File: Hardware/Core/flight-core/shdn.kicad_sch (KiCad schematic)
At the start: 19 parts, among them J101 Conn_01x02, J21 Conn_01x02, J22 Conn_01x02, J23 Conn_01x02, J24 Conn_01x02, J25 Conn_01x02, J26 Conn_01x02, J27 Conn_01x02, J28 Conn_01x02, J29 Conn_01x02, J3 Conn_01x02, J4 Conn_01x02, J6 Conn_01x02, J7 Conn_01x02, U10 LTV-356T, U65 LTV-356T

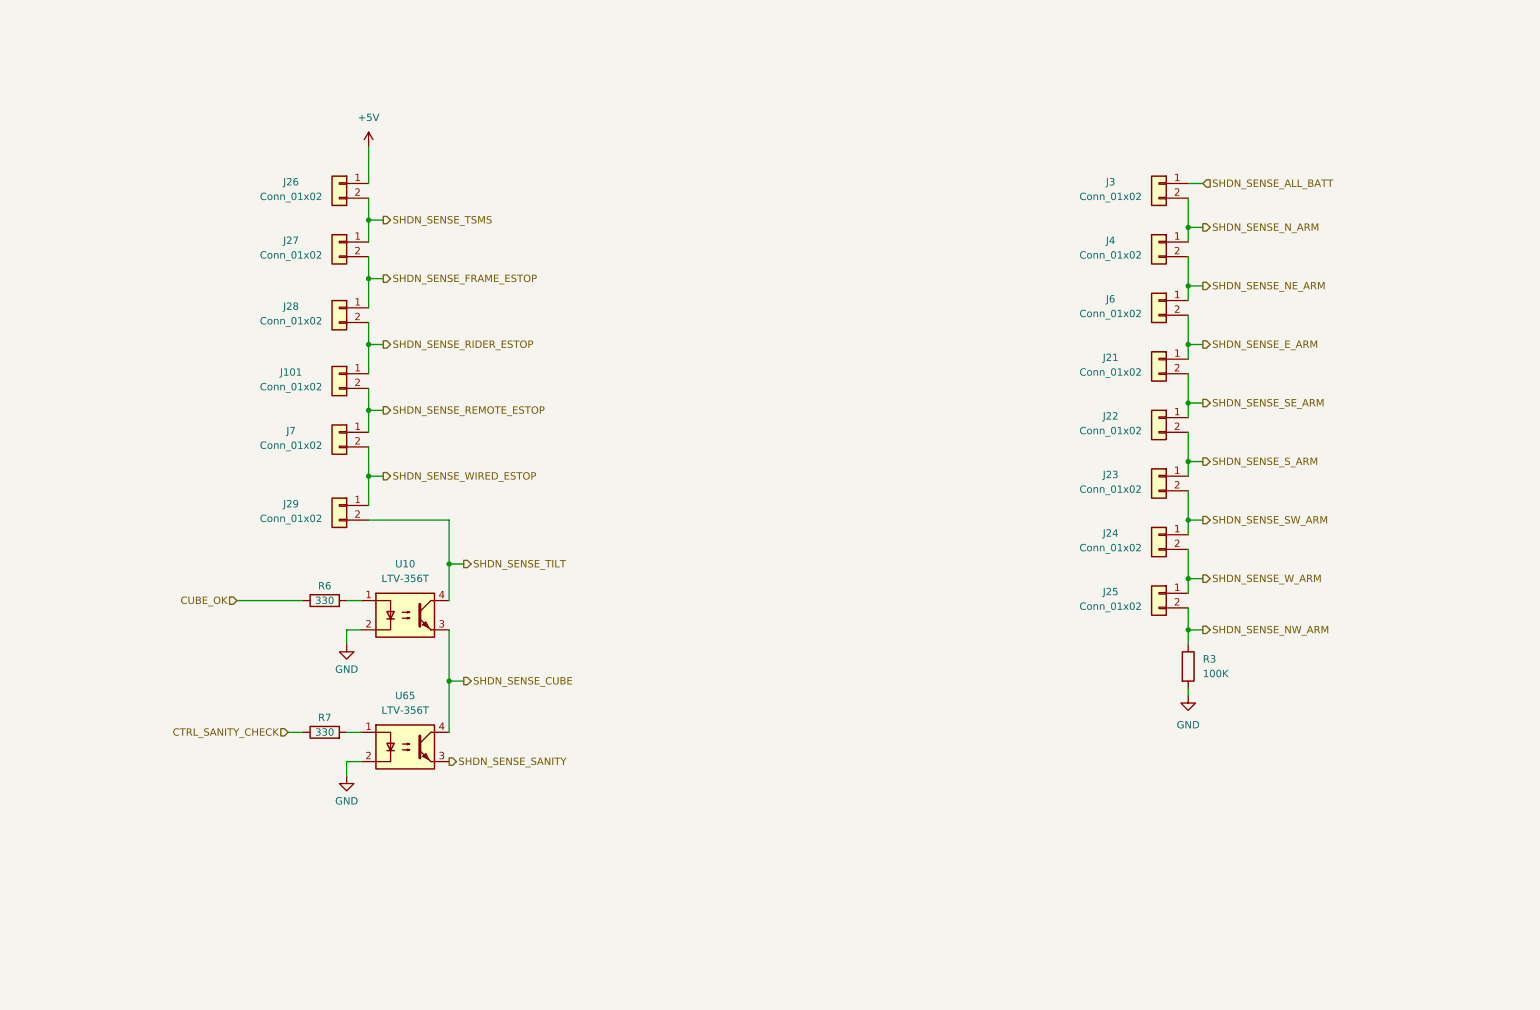
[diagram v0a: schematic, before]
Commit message: added all cube pins and corrected cube shdn node
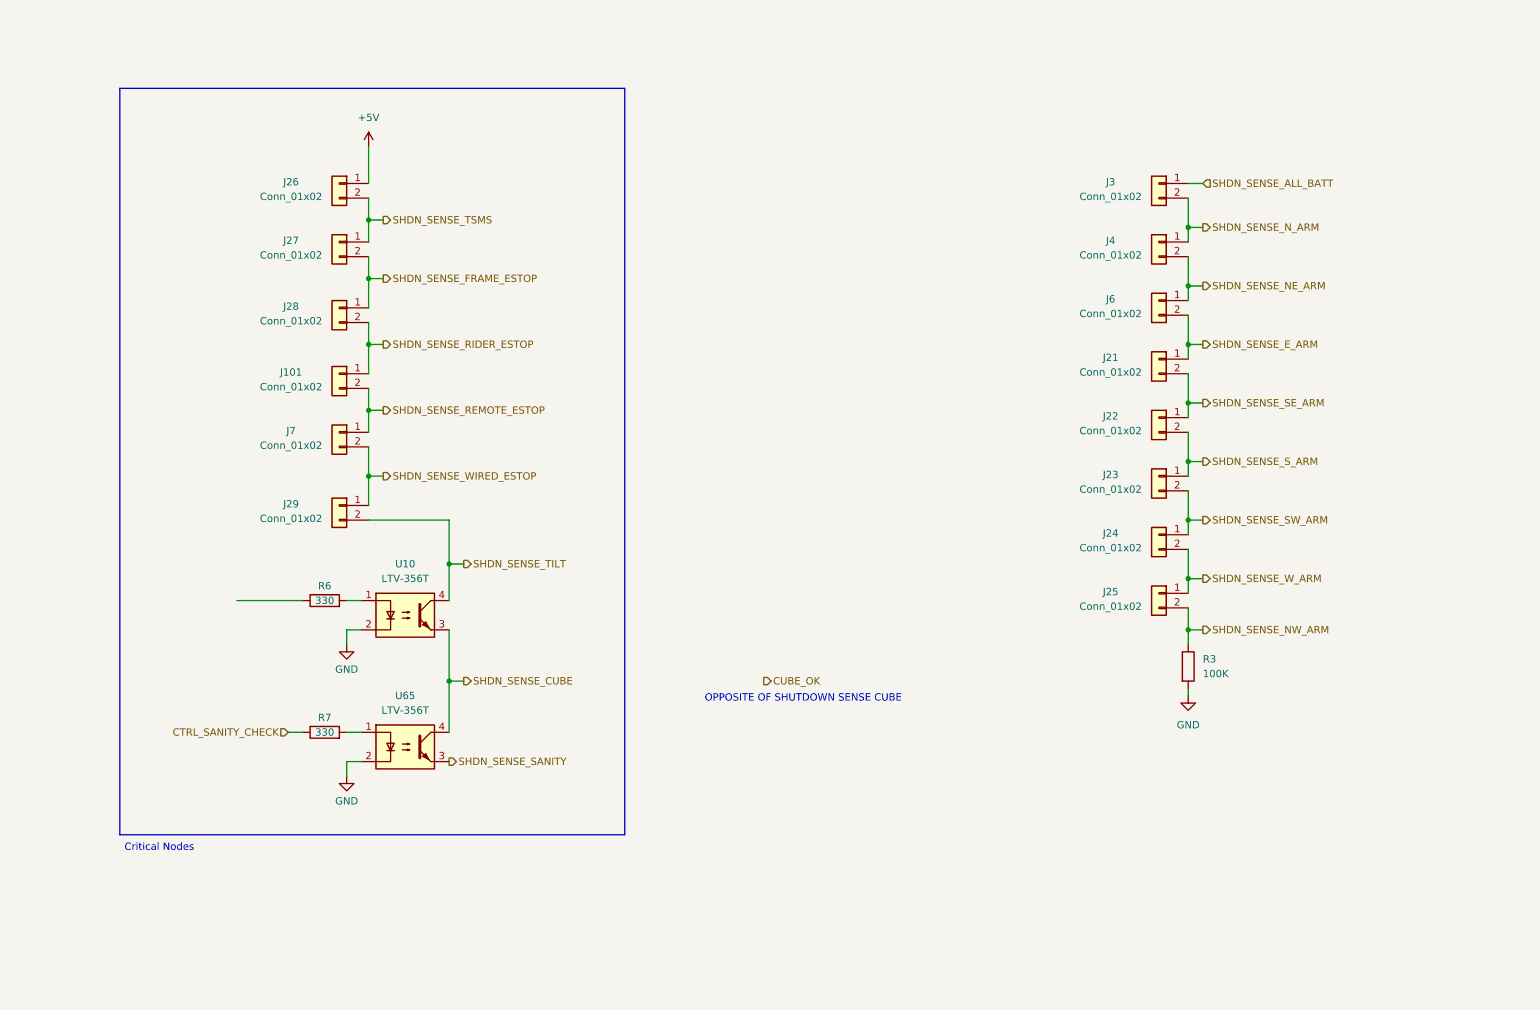
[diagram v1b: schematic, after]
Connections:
- net CUBE_OK: no longer R6.1
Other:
- note added: "Critical Nodes"
- note added: "OPPOSITE OF SHUTDOWN SENSE CUBE"
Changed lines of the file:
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@@
 	(generator_version "9.0")
 	(paper "A4")
+	(rectangle
+		(start 34.29 27.94)
+		(end 121.92 157.48)
+		(stroke
+			(width 0)
+			(type default)
+		)
+		(fill
+			(type none)
+		)
+	)
+	(text "OPPOSITE OF SHUTDOWN SENSE CUBE"
+		(exclude_from_sim no)
+		(at 152.908 133.858 0)
+		(effects
+			(font
+				(size 1.27 1.27)
+			)
+		)
+	)
+	(text "Critical Nodes"
+		(exclude_from_sim no)
+		(at 41.148 159.766 0)
+		(effects
+			(font
+				(size 1.27 1.27)
+			)
+		)
+	)
 	(junction
 		(at 219.71 72.39)
@@
 	)
 	(hierarchical_label "CUBE_OK"
-		(shape input)
-		(at 54.61 116.84 180)
+		(shape output)
+		(at 146.05 130.81 0)
 		(effects
 			(font
 				(size 1.27 1.27)
 			)
-			(justify right)
-		)
-	)
+			(justify left)
+		)
+	)

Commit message: reordered shutdown nodes
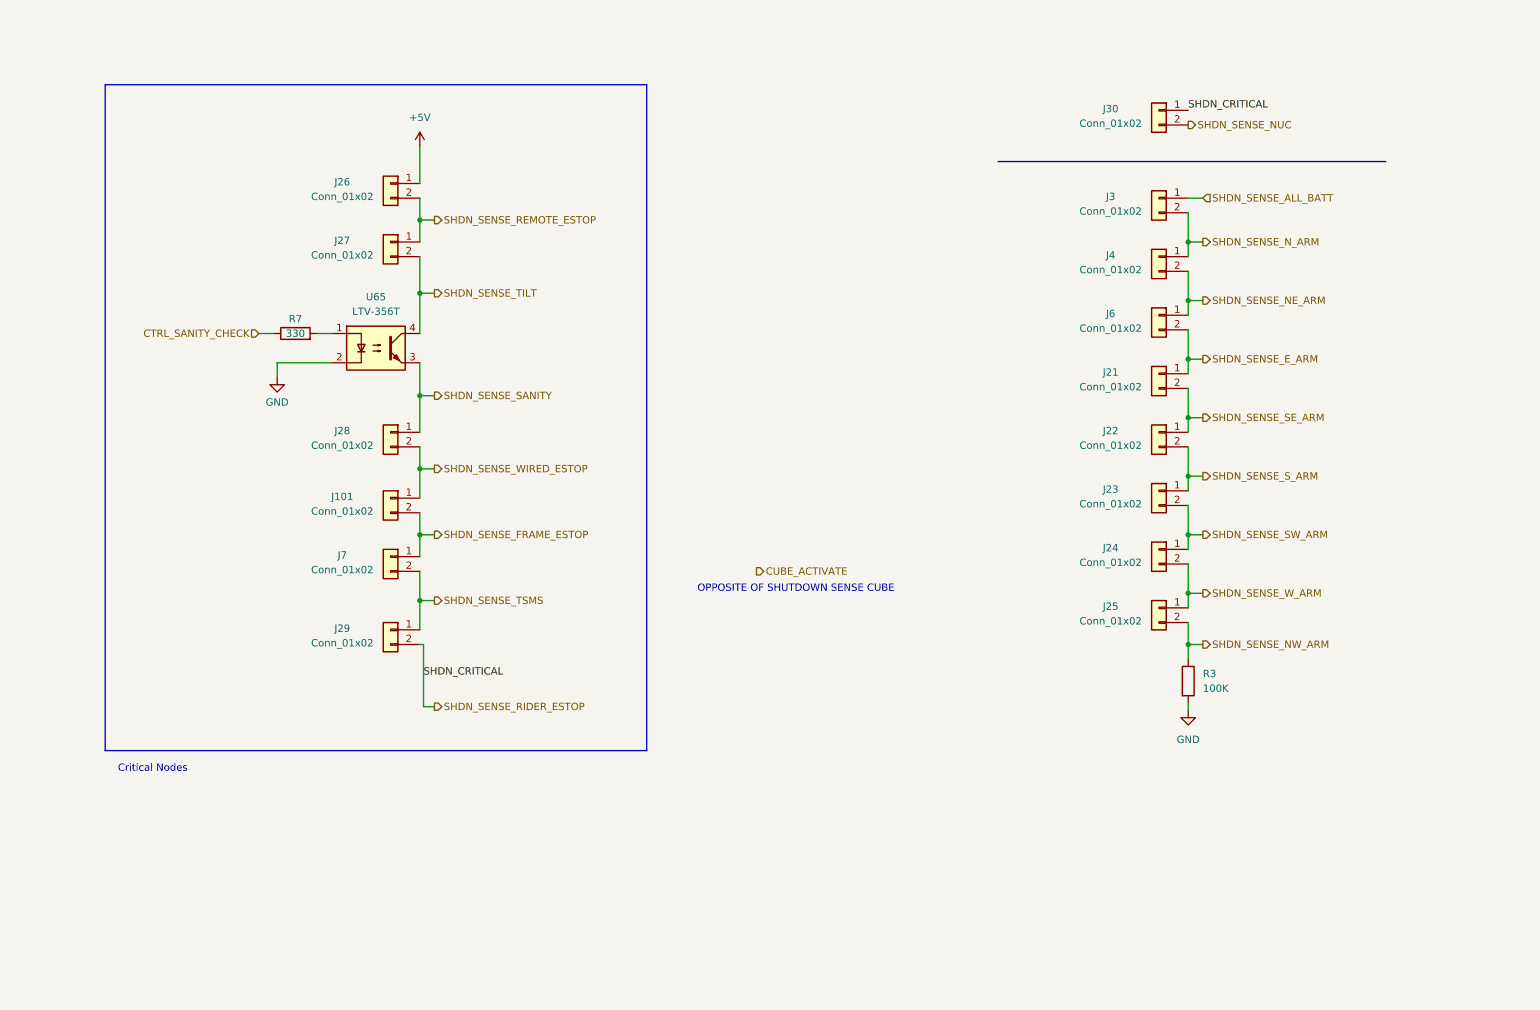
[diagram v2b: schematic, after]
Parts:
- removed R6: 330, OEM:R_0603_1608Metric, symbol OEM:1KR
- removed U10: LTV-356T, Package_SO:SO-4_4.4x3.6mm_P2.54mm, symbol Isolator:LTV-356T
- added J30: Conn_01x02, symbol Connector_Generic:Conn_01x02
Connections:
- net SHDN_SENSE_CUBE is gone; now on net SHDN_SENSE_TILT: U65.4
- net SHDN_SENSE_FRAME_ESTOP: now also J101.2 (Pin_2), J7.1 (Pin_1); no longer J27.2 (Pin_2), J28.1 (Pin_1)
- net SHDN_SENSE_REMOTE_ESTOP: now also J26.2 (Pin_2), J27.1 (Pin_1); no longer J101.2 (Pin_2), J7.1 (Pin_1)
- net SHDN_SENSE_RIDER_ESTOP: now also J29.2 (Pin_2), J30.1 (Pin_1); no longer J101.1 (Pin_1), J28.2 (Pin_2)
- net SHDN_SENSE_SANITY: now also J28.1 (Pin_1)
- net SHDN_SENSE_TILT: now also J27.2 (Pin_2); no longer J29.2 (Pin_2)
- net SHDN_SENSE_TSMS: now also J29.1 (Pin_1), J7.2 (Pin_2); no longer J26.2 (Pin_2), J27.1 (Pin_1)
- net SHDN_SENSE_WIRED_ESTOP: now also J101.1 (Pin_1), J28.2 (Pin_2); no longer J29.1 (Pin_1), J7.2 (Pin_2)
- new net SHDN_SENSE_NUC: J30.2 (Pin_2)
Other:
- moved on the sheet: J101, J21, J22, J23, J24, J25, J26, J27, J28, J29, J3, J4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

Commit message: top sheet reorg
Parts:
- added Q16: MMBF170, TO_SOT_Packages_SMD:SOT-23, symbol formula:MMBF170
- added R97: 100K, footprints:R_0805_OEM, symbol formula:R_100K
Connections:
- net +5V: now also R97.1
- net CUBE_ACTIVATE: now also Q16.3 (D), R97.2
- net GND: now also Q16.2 (S)
- net SHDN_SENSE_NW_ARM: now also Q16.1 (G)
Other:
- note added: "BATTERY SHDNS (x4)"
- note added: "CRITICAL NODES"
- note removed: "Critical Nodes"
- note removed: "OPPOSITE OF SHUTDOWN SENSE CUBE"
- moved on the sheet: J21, J22, J23, J24, J25, J3, J30, J4, J6, R3

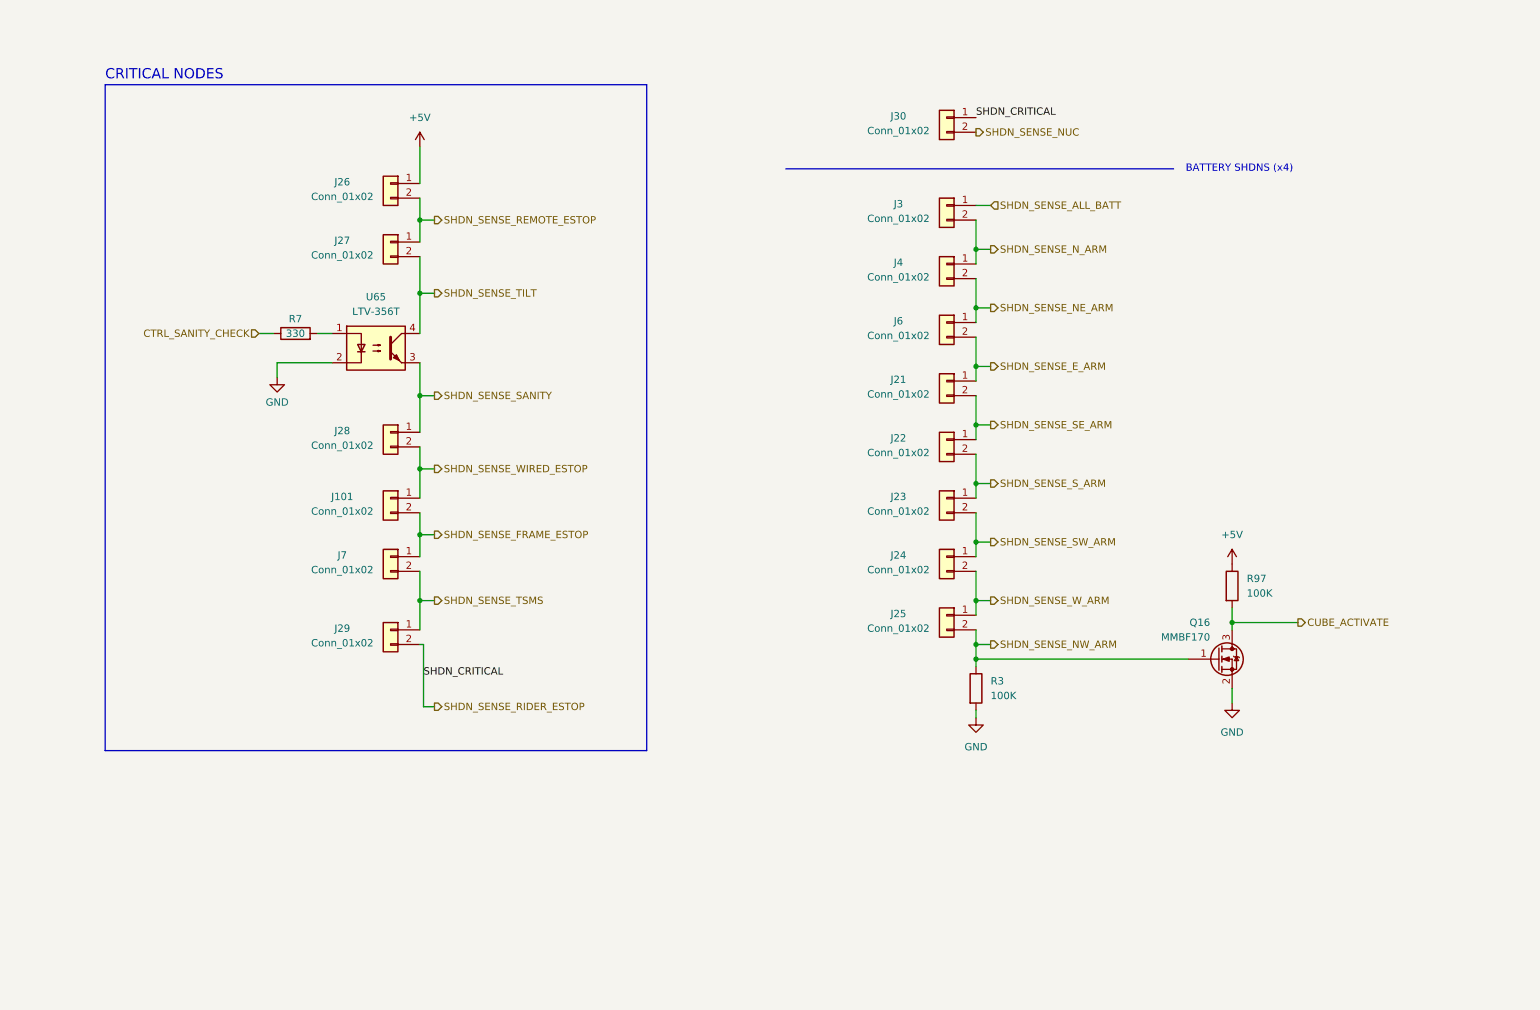
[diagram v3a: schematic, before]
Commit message: updated shutdown and some aux circuits
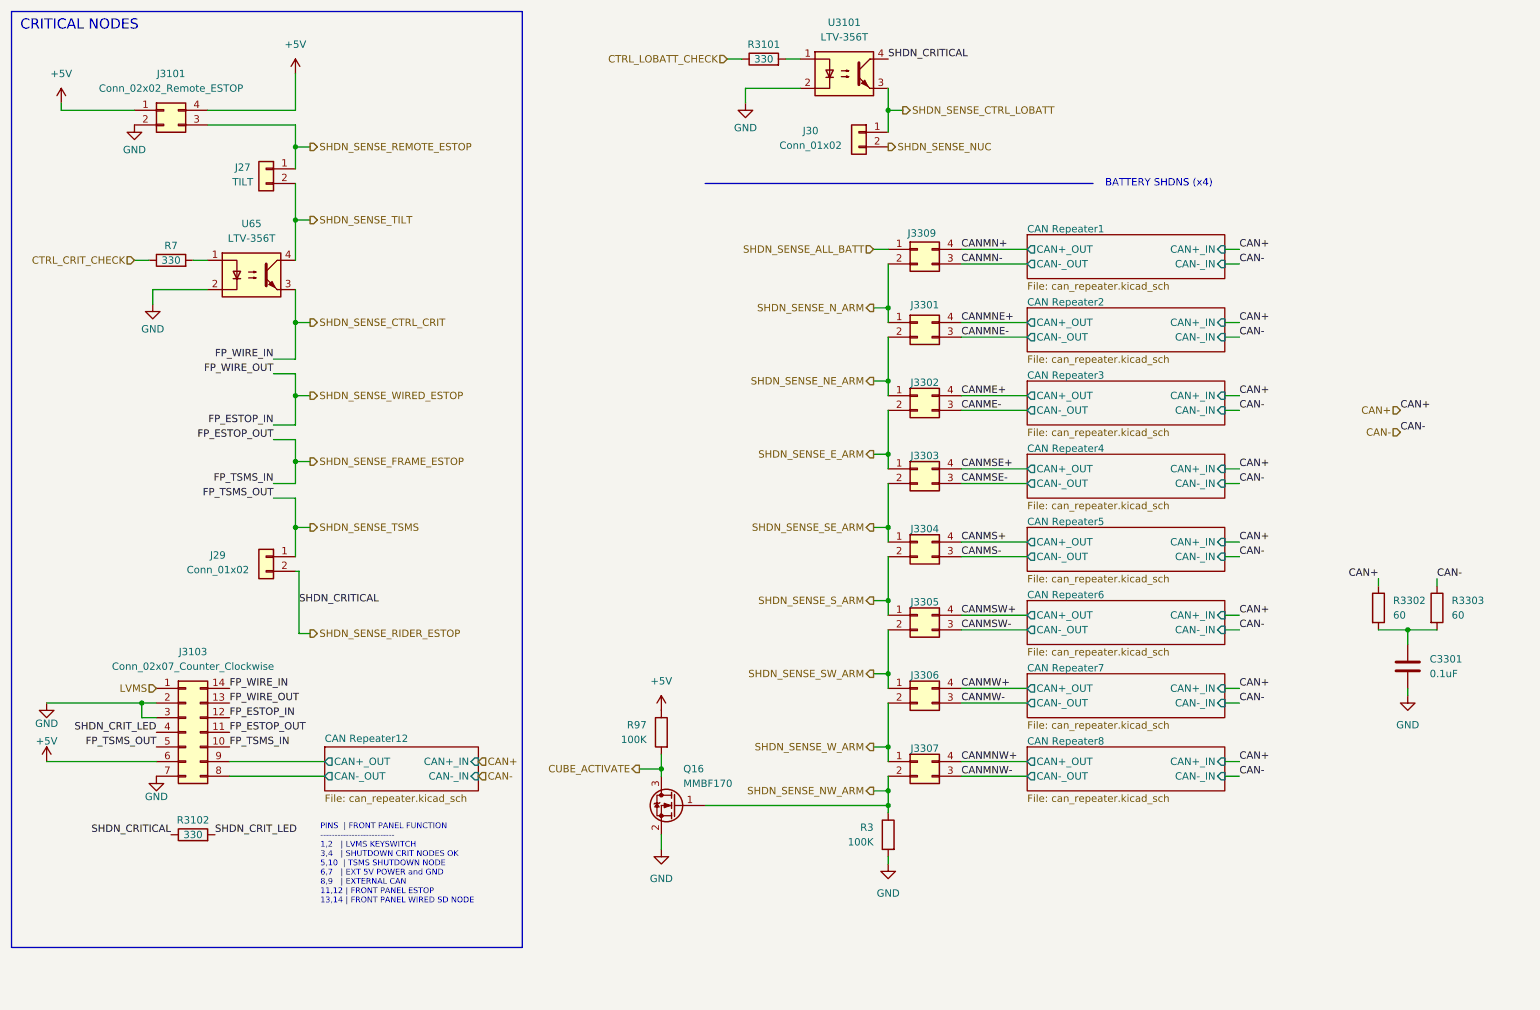
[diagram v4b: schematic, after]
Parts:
- removed J101, J21, J22, J23, J24, J25, J26, J28, J3, J4, J6, J7: Conn_01x02, symbol Connector_Generic:Conn_01x02
- added C3301: 0.1uF, footprints:C_0603_1608Metric, symbol OlinBAD:C_0.1uF_0603
- added J3101, J3301, J3302, J3303, J3304, J3305, J3306, J3307, J3309: Conn_02x02_Remote_ESTOP, Connector_Molex:Molex_Micro-Fit_3.0_43045-0400_2x02_P3.00mm_Horizontal, symbol Connector_Generic:Conn_02x02_Counter_Clockwise
- added J3103: Conn_02x07_Counter_Clockwise, symbol Connector_Generic:Conn_02x07_Counter_Clockwise
- added R3101, R3102: 330, OEM:R_0603_1608Metric, symbol OEM:1KR
- added R3302, R3303: 60, footprints:C_0603_1608Metric, symbol Device:R
- added U3101: LTV-356T, Package_SO:SO-4_4.4x3.6mm_P2.54mm, symbol Isolator:LTV-356T
- J27: value Conn_01x02 -> TILT
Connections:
- net +5V: now also J3101.1 (Pin_1), J3101.4 (Pin_4), J3103.6 (Pin_6)
- net GND: now also C3301.2, J3101.2 (Pin_2), J3103.2 (Pin_2), J3103.3 (Pin_3), J3103.7 (Pin_7), U3101.2
- net SHDN_SENSE_ALL_BATT: now also J3309.1 (Pin_1)
- net SHDN_SENSE_E_ARM: now also J3302.2 (Pin_2), J3303.1 (Pin_1)
- net SHDN_SENSE_FRAME_ESTOP: now also J3103.10 (Pin_10), J3103.11 (Pin_11)
- net SHDN_SENSE_NE_ARM: now also J3301.2 (Pin_2), J3302.1 (Pin_1)
- net SHDN_SENSE_NW_ARM: now also J3307.2 (Pin_2)
- net SHDN_SENSE_N_ARM: now also J3301.1 (Pin_1), J3309.2 (Pin_2)
- net SHDN_SENSE_REMOTE_ESTOP: now also J3101.3 (Pin_3)
- net SHDN_SENSE_RIDER_ESTOP: now also R3102.1, U3101.4; no longer J30.1 (Pin_1)
- net SHDN_SENSE_SE_ARM: now also J3303.2 (Pin_2), J3304.1 (Pin_1)
- net SHDN_SENSE_SW_ARM: now also J3305.2 (Pin_2), J3306.1 (Pin_1)
- net SHDN_SENSE_S_ARM: now also J3304.2 (Pin_2), J3305.1 (Pin_1)
- net SHDN_SENSE_TSMS: now also J3103.5 (Pin_5)
- net SHDN_SENSE_WIRED_ESTOP: now also J3103.12 (Pin_12), J3103.13 (Pin_13)
- net SHDN_SENSE_W_ARM: now also J3306.2 (Pin_2), J3307.1 (Pin_1)
- net CTRL_SANITY_CHECK renamed CTRL_CRIT_CHECK
- net SHDN_SENSE_SANITY renamed SHDN_SENSE_CTRL_CRIT
- net SHDN_SENSE_CTRL_CRIT: now also J3103.14 (Pin_14)
- new net: C3301.1, R3302.2, R3303.2
- new net: R3101.2, U3101.1
- new net CAN Repeater12/CAN+_OUT: J3103.9 (Pin_9)
- new net CAN Repeater12/CAN-_OUT: J3103.8 (Pin_8)
- new net CAN+: R3302.1
- new net CAN-: R3303.1
- new net CANME+: J3302.4 (Pin_4)
- new net CANME-: J3302.3 (Pin_3)
- new net CANMN+: J3309.4 (Pin_4)
- new net CANMN-: J3309.3 (Pin_3)
- new net CANMNE+: J3301.4 (Pin_4)
- new net CANMNE-: J3301.3 (Pin_3)
- new net CANMNW+: J3307.4 (Pin_4)
- new net CANMNW-: J3307.3 (Pin_3)
- new net CANMS+: J3304.4 (Pin_4)
- new net CANMS-: J3304.3 (Pin_3)
- new net CANMSE+: J3303.4 (Pin_4)
- new net CANMSE-: J3303.3 (Pin_3)
- new net CANMSW+: J3305.4 (Pin_4)
- new net CANMSW-: J3305.3 (Pin_3)
- new net CANMW+: J3306.4 (Pin_4)
- new net CANMW-: J3306.3 (Pin_3)
- new net CTRL_LOBATT_CHECK: R3101.1
- new net LVMS: J3103.1 (Pin_1)
- new net SHDN_CRIT_LED: J3103.4 (Pin_4), R3102.2
- new net SHDN_SENSE_CTRL_LOBATT: J30.1 (Pin_1), U3101.3
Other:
- added sheet CAN Repeater1 (can_repeater.kicad_sch)
- added sheet CAN Repeater12 (can_repeater.kicad_sch)
- added sheet CAN Repeater2 (can_repeater.kicad_sch)
- added sheet CAN Repeater3 (can_repeater.kicad_sch)
- added sheet CAN Repeater4 (can_repeater.kicad_sch)
- added sheet CAN Repeater5 (can_repeater.kicad_sch)
- added sheet CAN Repeater6 (can_repeater.kicad_sch)
- added sheet CAN Repeater7 (can_repeater.kicad_sch)
- added sheet CAN Repeater8 (can_repeater.kicad_sch)
- note added: "PINS | FRONT PANEL FUNCTION -------------------------- 1,2 | LVMS KEYSWITCH 3,4 | SHUTDOWN CRIT NODES OK 5,10 | TSMS SHUTDOWN NODE 6,7 | EXT 5V POWER and GND 8,9 | EXTERNAL CAN 11,12 | FRONT PANEL ESTOP 13,14 | FRONT PANEL WIRED SD NODE"
- moved on the sheet: J27, J29, J30, Q16, R3, R7, R97, U65

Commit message: updated all top sheets
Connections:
- net CTRL_LOBATT_CHECK renamed CTRL_NONCRIT_CHECK
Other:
- moved on the sheet: C3301, J27, J29, J30, J3101, J3103, J3301, J3302, J3303, J3304, J3305, J3306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
